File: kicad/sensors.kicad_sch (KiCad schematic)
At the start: 3 parts, among them U10 BMM350, U11 BMP581, U4 ICM-45686

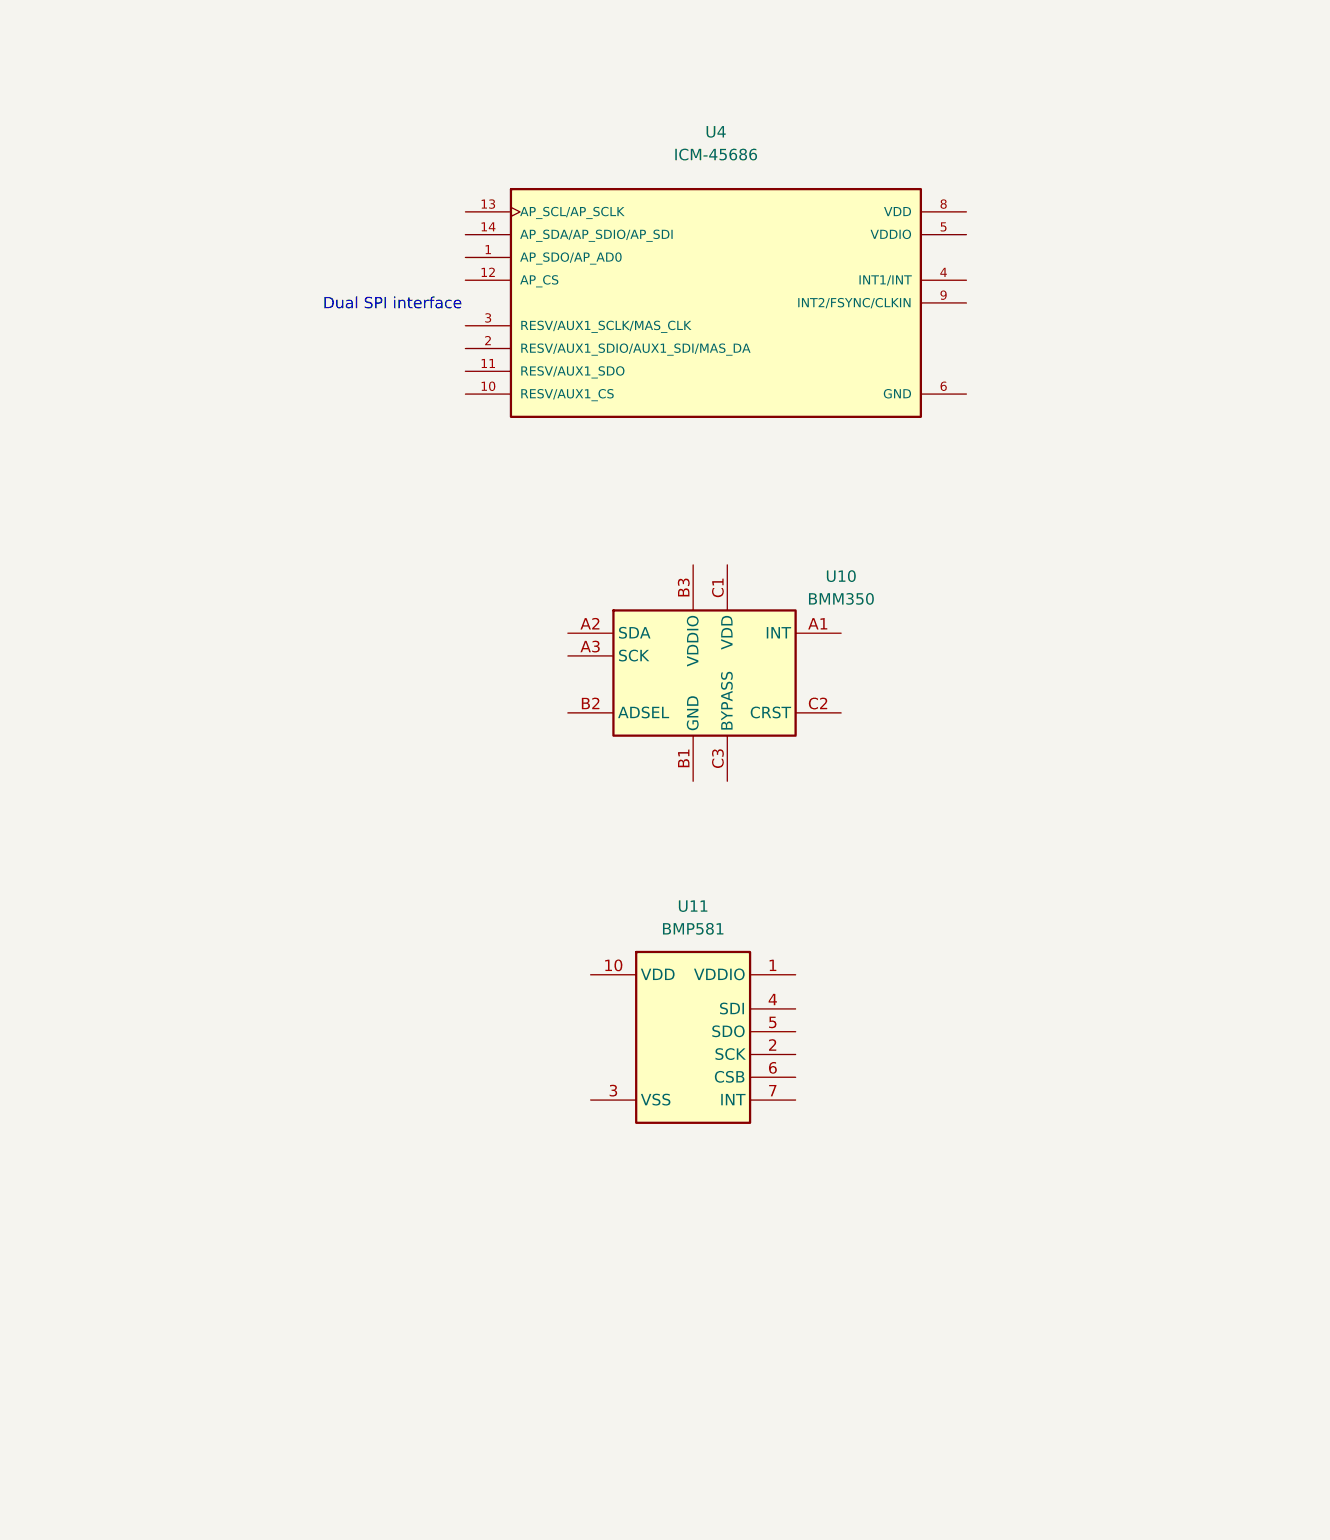
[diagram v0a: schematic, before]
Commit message: Updated schematics and BOM.
- Finished power supply schematics
- Added power schematic around MCXN
- Assigned MCXN pins
- Created board-to-board schematic and assigned pins to DF40T board-to-board connector
- Added correct sensors, finished sensor schematic
- Updated parts in communication schematic
- Added all part numbers etc in parts parameters
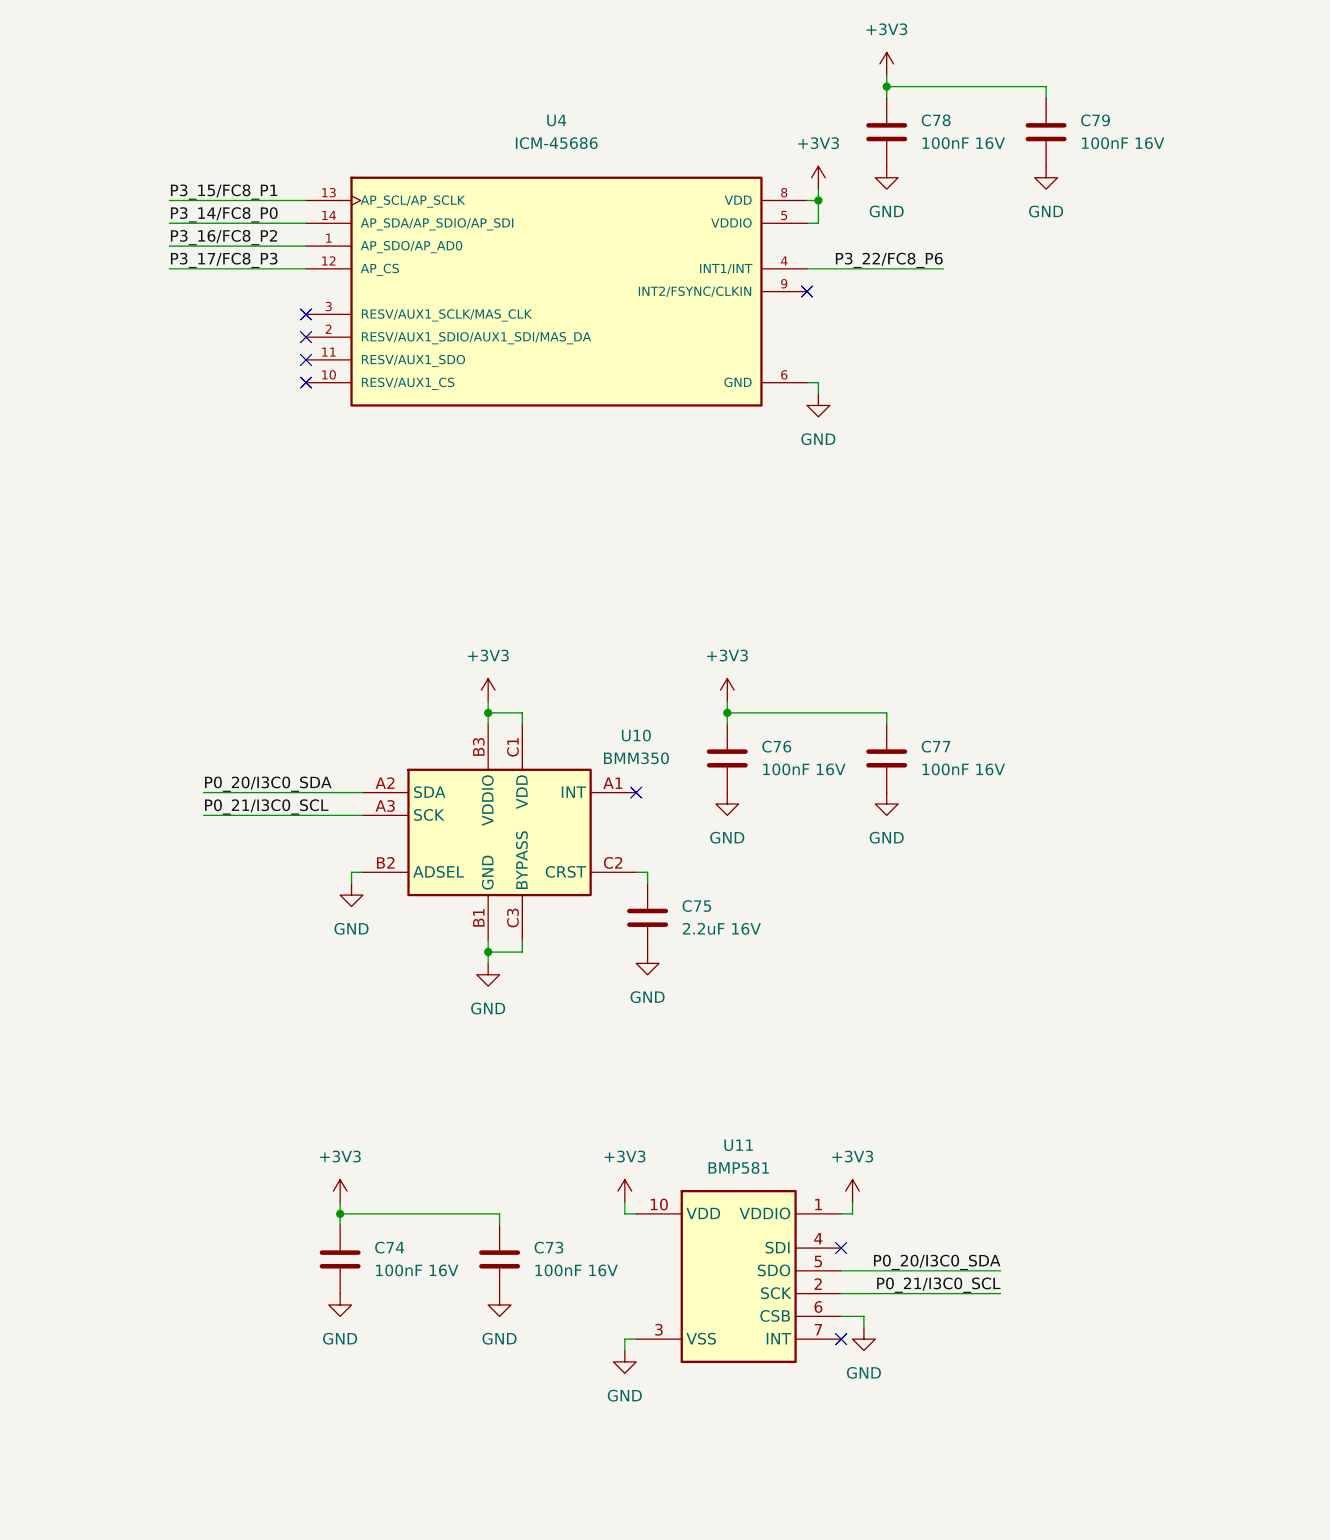
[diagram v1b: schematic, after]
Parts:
- added C73, C74, C76, C77, C78, C79: 100nF 16V, Capacitor_SMD:C_0402_1005Metric, symbol Device:C
- added C75: 2.2uF 16V, Capacitor_SMD:C_0805_2012Metric, symbol Device:C
- U10: MF (none) -> Bosch Sensortec; MFPN (none) -> BMM350; Supplier (none) -> JLCPCB; Supplier PN (none) -> C17225907
- U11: MF (none) -> Bosch Sensortec; MFPN (none) -> BMP581; Supplier (none) -> JLCPCB; Supplier PN (none) -> C5362283
- U4: MF (none) -> TDK InvenSense; MFPN (none) -> ICM-45686; Supplier (none) -> JLCPCB; Supplier PN (none) -> C22459454
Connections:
- net P3_16/FC8_P2: now reaches U4.1 (AP_SDO/AP_AD0)
- net P3_17/FC8_P3: now reaches U4.12 (AP_CS)
- net P3_15/FC8_P1: now reaches U4.13 (AP_SCL/AP_SCLK)
- net P3_14/FC8_P0: now reaches U4.14 (AP_SDA/AP_SDIO/AP_SDI)
- net P3_22/FC8_P6: now reaches U4.4 (INT1/INT)
- net +3V3: now reaches U4.5 (VDDIO)
- net +3V3: now also U10.B3 (VDDIO), U10.C1 (VDD), U11.1 (VDDIO), U11.10 (VDD), U4.8 (VDD), C73.2, C74.2, C76.1, C77.1, C78.1, C79.1
- net GND: now reaches U4.6 (GND)
- net GND: now also U10.B1 (GND), U10.B2 (ADSEL), U10.C3 (BYPASS), U11.3 (VSS), U11.6 (CSB), U11.8 (VSS), U11.9 (VSS), C73.1, C74.1, C75.2, C76.2, C77.2, C78.2, C79.2
- net P0_21/I3C0_SCL: now reaches U11.2 (SCK)
- net P0_21/I3C0_SCL: now also U10.A3 (SCK)
- net P0_20/I3C0_SDA: now reaches U11.5 (SDO)
- net P0_20/I3C0_SDA: now also U10.A2 (SDA)
- net at U10.C2 (CRST): now also C75.1
- no-connect marks 0 -> 8
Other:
- note removed: "Dual SPI interface"
- moved on the sheet: U10, U11, U4

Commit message: Updated schematic and started on layout
- Implemented schematic changes after feedback:
	- BMM350 VDD is 1.8V
	- Replaced net labels with global labels for page references
	- Added 1uF cap to SK9822-EC20
- Added rev-RMII configuration for TJA1103 and DNP resistor to put it in slave mode
- Added TJA1103 PHY address info
- Changed decoupling caps for MCXN to smallest possible packages
- Added traces and vias at MCXN according to guidelines
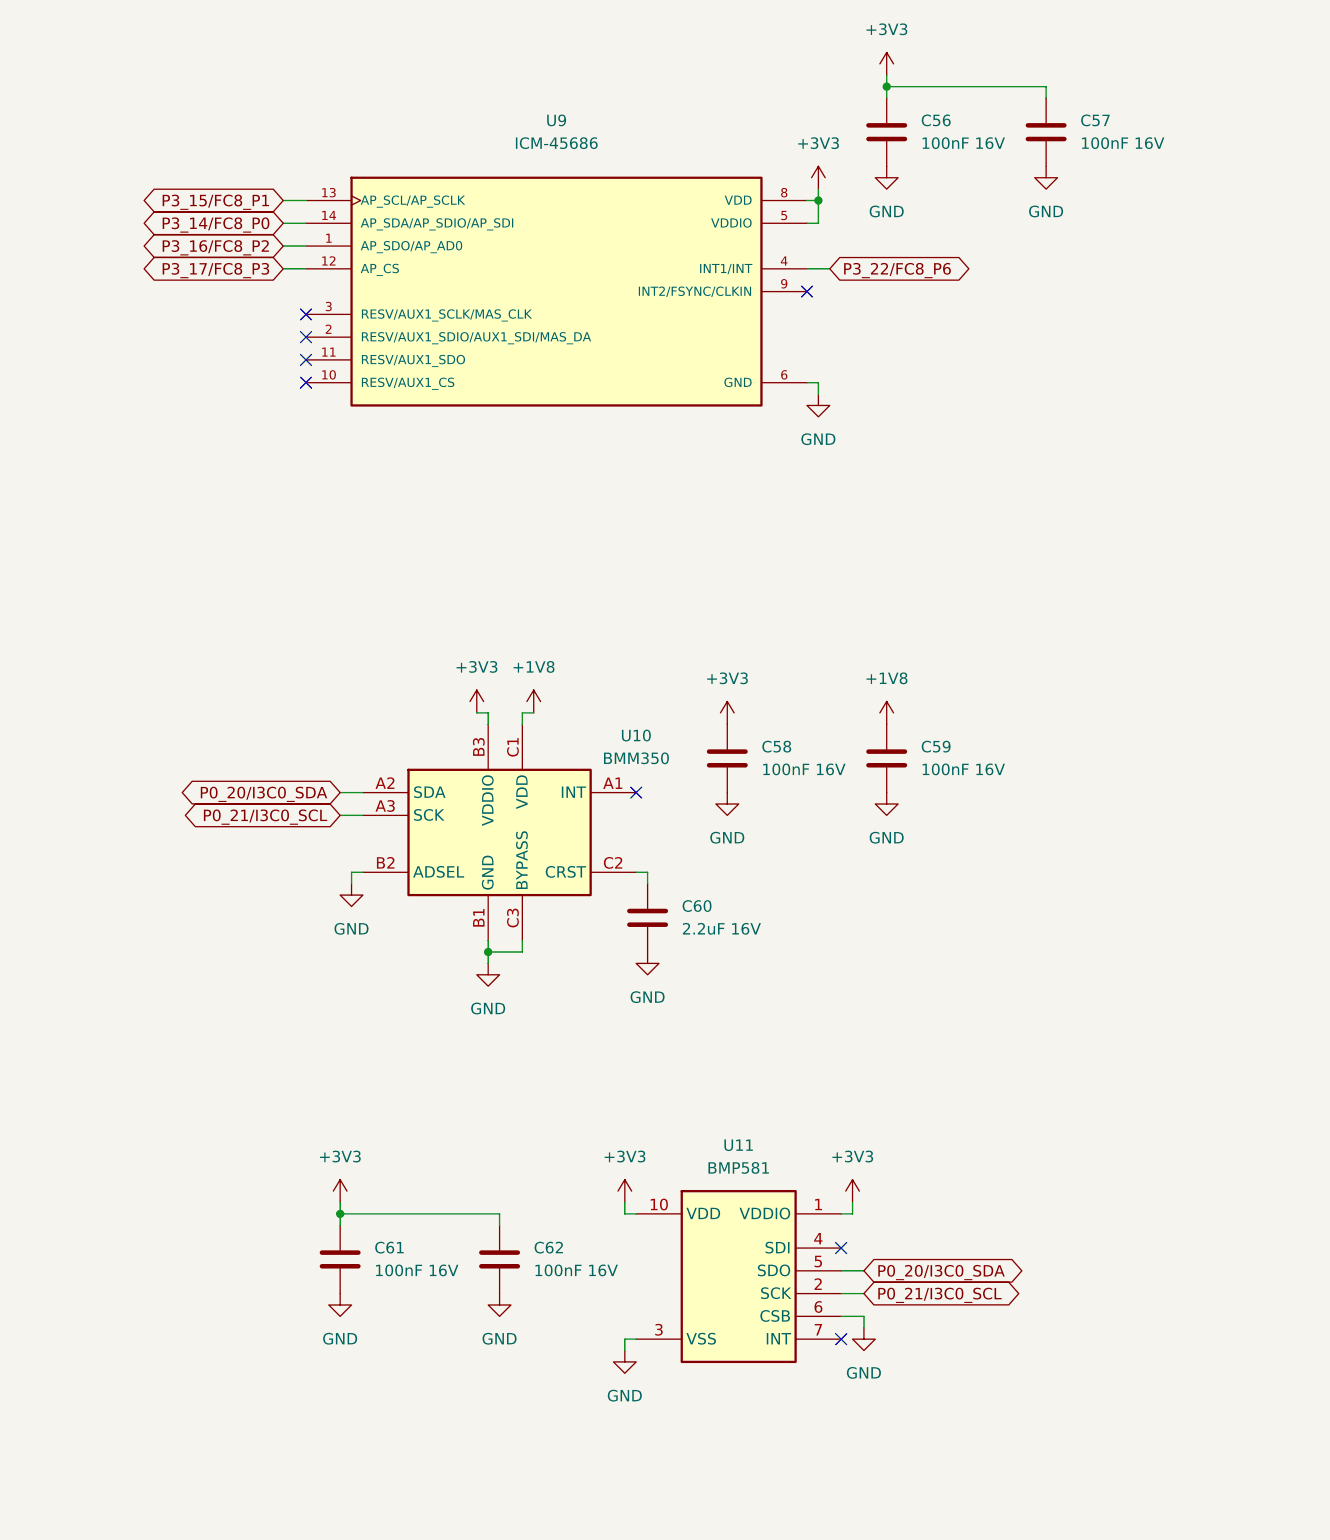
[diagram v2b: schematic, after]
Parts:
- U9: renamed from U4; MANUFACTURER TDK InvenSense -> (none); MAXIMUM_PACKAGE_HEIGHT 0.86mm -> (none); PARTREV 0.2 -> (none); STANDARD Manufacturer Recommendations -> (none)
- renumbered C78 to C56, C79 to C57, C76 to C58, C77 to C59, C75 to C60, C74 to C61, C73 to C62
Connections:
- net +3V3: no longer C59.1, U10.C1 (VDD)
- new net +1V8: C59.1, U10.C1 (VDD)

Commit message: Updated schematic after feedback from Jari
- Finished schematic after feedback from Jari. It is at a finished state, can be reviewed by whole team now.
- Layouted MCXN with decoupling caps.
- Layouted Base100-T1 ethernet phy.
- Layouted the power supply a bit.
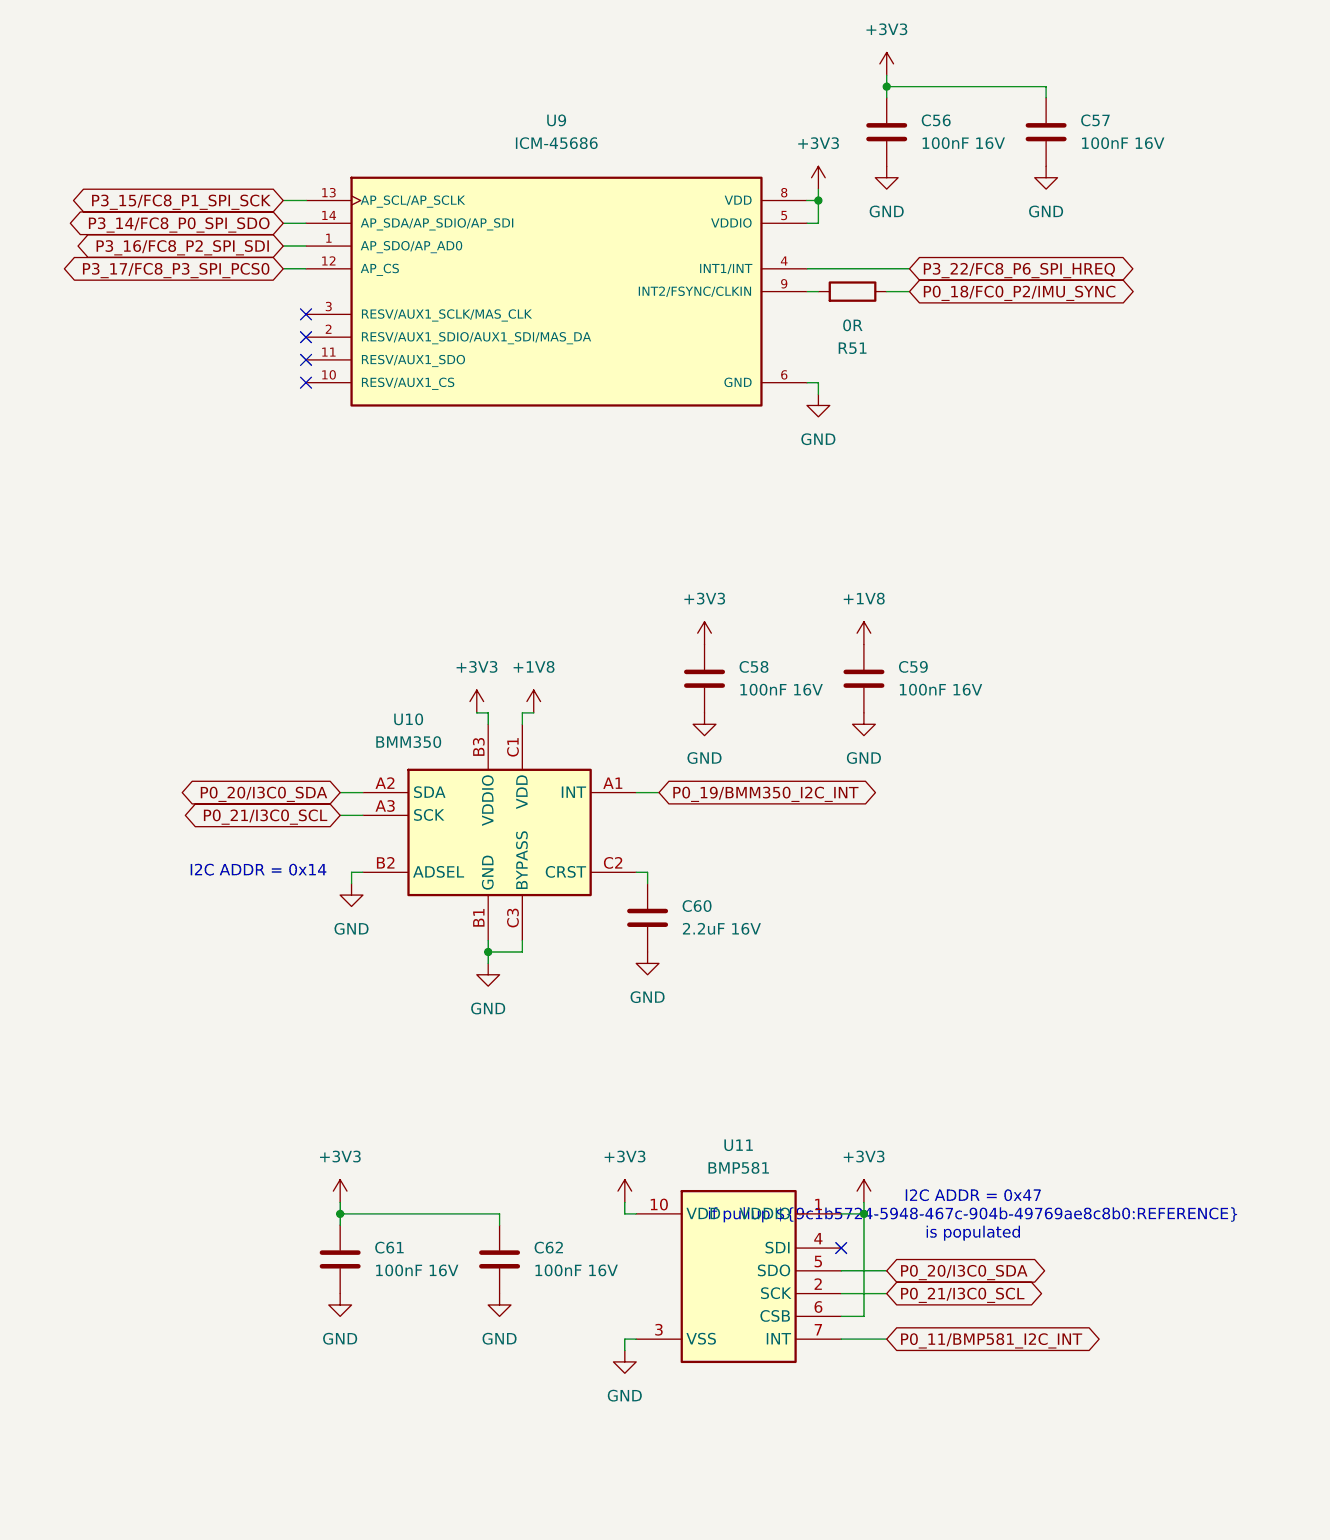
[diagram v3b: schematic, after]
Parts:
- added R51: 0R, symbol Device:R
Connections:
- net +3V3: now also U11.6 (CSB)
- net GND: no longer U11.6 (CSB)
- net at U9.9 (INT2/FSYNC/CLKIN): now also R51.2
- net P0_11/BMP581_I2C_INT: now reaches U11.7 (INT)
- net P0_19/BMM350_I2C_INT: now reaches U10.A1 (INT)
- net P3_14/FC8_P0 renamed P3_14/FC8_P0_SPI_SDO
- net P3_15/FC8_P1 renamed P3_15/FC8_P1_SPI_SCK
- net P3_16/FC8_P2 renamed P3_16/FC8_P2_SPI_SDI
- net P3_17/FC8_P3 renamed P3_17/FC8_P3_SPI_PCS0
- net P3_22/FC8_P6 renamed P3_22/FC8_P6_SPI_HREQ
- new net P0_18/FC0_P2/IMU_SYNC: R51.1
- no-connect marks 8 -> 5
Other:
- note added: "I2C ADDR = 0x14"
- note added: "I2C ADDR = 0x47 if pullup ${9c1b5724-5948-467c-904b-49769ae8c8b0:REFERENCE} is populated"
- title: MR-MCXN-T1 Sensor hub -> MR-MCXN-T1 Sensor Node
- moved on the sheet: C58, C59
